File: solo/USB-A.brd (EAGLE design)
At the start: 43.8 x 16 mm, 26 parts, among them U1 USB_TRACES

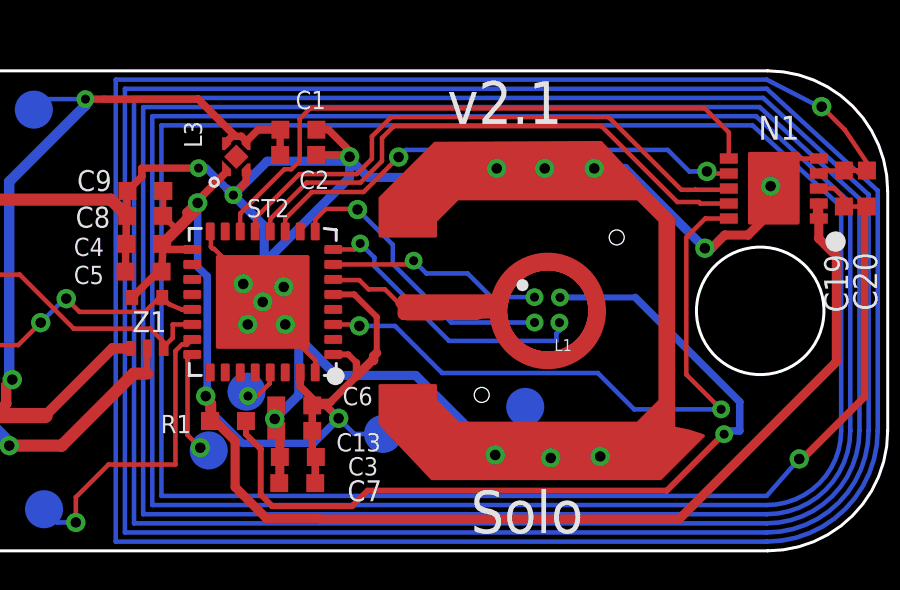
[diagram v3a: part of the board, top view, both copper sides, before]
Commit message: go back to using old LED
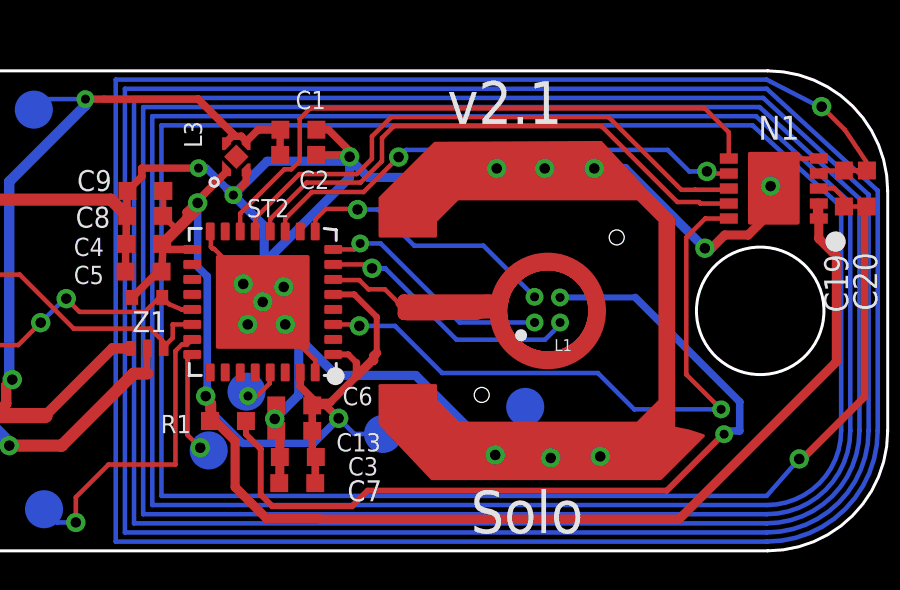
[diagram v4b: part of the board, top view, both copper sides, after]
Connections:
- net N$10: now also L1.P$2; no longer L1.P$3
- net N$13: now also L1.P$1; no longer L1.P$2
- net N$14: now also L1.P$3; no longer L1.P$1
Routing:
- net N$14: track 7.34 -> 9.46 mm
- net N$10: track 9.79 -> 7.89 mm
- net N$13: track 9.81 -> 9.08 mm
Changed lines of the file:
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@@
 </layers>
 <board>
-<fusionsync huburn="a.cGVyc29uYWw6dWUyYjdlZTY2" projecturn="a.cGVyc29uYWw6dWUyYjdlZTY2IzIwMTgwNDI5MTI5NzYxOTgx" f3durn="urn:adsk.wipprod:dm.lineage:j4HlS92DQ3aJOR3aA8LYVQ" pcbguid="4a57c918-3773-4eb5-941a-4639588bec0f" lastpulledtime="" lastsyncedchangeguid="8ec78108-e873-5518-f778-6aed3102f0ab"/>
+<fusionsync huburn="a.cGVyc29uYWw6dWUyYjdlZTY2" projecturn="a.cGVyc29uYWw6dWUyYjdlZTY2IzIwMTgwNDI5MTI5NzYxOTgx" f3durn="urn:adsk.wipprod:dm.lineage:j4HlS92DQ3aJOR3aA8LYVQ" pcbguid="4a57c918-3773-4eb5-941a-4639588bec0f" lastpulledtime="" lastsyncedchangeguid="35127d9d-d647-938f-e0ae-f05b0d64aa73"/>
 <plain>
 <rectangle x1="3.6" y1="49.05" x2="4.4" y2="49.25" layer="41"/>
@@
 <attribute name="NAME" x="20.415" y="51.685" size="0.7" layer="25" ratio="15" rot="R180"/>
 </element>
-<element name="L1" library="efm-fido" library_urn="urn:adsk.eagle:library:4245354" package="CL-505S-X-SD-T" package3d_urn="urn:adsk.eagle:package:4878740/7" value="RGB_LED_1X1CL-505S-X-SD-T" x="35.36" y="47.45" smashed="yes" rot="R180">
+<element name="L1" library="efm-fido" library_urn="urn:adsk.eagle:library:4245354" package="CL-505S-X-SD-T" package3d_urn="urn:adsk.eagle:package:4878740/8" value="RGB_LED_1X1CL-505S-X-SD-T" x="35.36" y="47.45" smashed="yes" rot="R180">
 <attribute name="NAME" x="35.76" y="46.05" size="0.4" layer="21" rot="R180"/>
 </element>
@@
 <wire x1="28.5" y1="49.04" x2="28.7" y2="49.24" width="0.1524" layer="1"/>
 <via x="28.7" y="49.24" extent="1-16" drill="0.3"/>
-<wire x1="28.7" y1="49.24" x2="28.78" y2="49.24" width="0.1524" layer="16"/>
-<via x="35.34" y="46.6" extent="1-16" drill="0.3"/>
-<wire x1="28.7" y1="49.24" x2="29.1714" y2="48.7686" width="0.1524" layer="16"/>
-<wire x1="29.1714" y1="48.7686" x2="29.1714" y2="48.48104375" width="0.1524" layer="16"/>
-<wire x1="29.1714" y1="48.48104375" x2="31.66244375" y2="45.99" width="0.1524" layer="16"/>
-<wire x1="31.66244375" y1="45.99" x2="35.24" y2="45.99" width="0.1524" layer="16"/>
-<wire x1="35.24" y1="45.99" x2="35.24" y2="46.24" width="0.1524" layer="16"/>
-<contactref element="L1" pad="P$3"/>
-<wire x1="35.24" y1="46.24" x2="35.34" y2="46.34" width="0.1524" layer="16"/>
-<wire x1="35.34" y1="46.34" x2="35.34" y2="46.6" width="0.1524" layer="16"/>
-<wire x1="35.36" y1="46.6" x2="35.34" y2="46.6" width="0.1524" layer="1"/>
+<via x="34.513" y="46.605" extent="1-16" drill="0.3"/>
+<contactref element="L1" pad="P$2"/>
+<wire x1="34.513" y1="46.605" x2="32.0157875" y2="46.605" width="0.1524" layer="16"/>
+<wire x1="32.0157875" y1="46.605" x2="29.3807875" y2="49.24" width="0.1524" layer="16"/>
+<wire x1="29.3807875" y1="49.24" x2="28.7" y2="49.24" width="0.1524" layer="16"/>
+<wire x1="34.513" y1="46.605" x2="34.51" y2="46.6" width="0" layer="19" extent="1-1"/>
 </signal>
 <signal name="N$13">
@@
 <via x="28.61" y="50.37" extent="1-16" drill="0.35"/>
 <wire x1="27.2" y1="49.64" x2="27.2" y2="50.04" width="0.1524" layer="1"/>
-<via x="34.512" y="46.604" extent="1-16" drill="0.3"/>
-<contactref element="L1" pad="P$2"/>
-<wire x1="28.61" y1="50.37" x2="29.7858" y2="49.1942" width="0.1524" layer="16"/>
-<wire x1="29.7858" y1="49.1942" x2="29.7858" y2="48.5545625" width="0.1524" layer="16"/>
-<wire x1="29.7858" y1="48.5545625" x2="31.7363625" y2="46.604" width="0.1524" layer="16"/>
-<wire x1="31.7363625" y1="46.604" x2="34.512" y2="46.604" width="0.1524" layer="16"/>
-<wire x1="34.512" y1="46.604" x2="34.51" y2="46.6" width="0" layer="19" extent="1-1"/>
+<via x="34.512" y="47.46" extent="1-16" drill="0.3"/>
+<wire x1="29.294" y1="50.37" x2="30.4998" y2="49.1642" width="0.1524" layer="16"/>
+<wire x1="28.61" y1="50.37" x2="29.294" y2="50.37" width="0.1524" layer="16"/>
+<contactref element="L1" pad="P$1"/>
+<wire x1="30.4998" y1="49.1642" x2="32.8078" y2="49.1642" width="0.1524" layer="16"/>
+<wire x1="32.8078" y1="49.1642" x2="34.512" y2="47.46" width="0.1524" layer="16"/>
+<wire x1="34.512" y1="47.46" x2="34.51" y2="47.45" width="0" layer="19" extent="1-1"/>
 </signal>
 <signal name="N$14">
 <contactref element="ST2" pad="7"/>
-<wire x1="27.8" y1="48.54" x2="30.481" y2="48.54" width="0.1524" layer="1"/>
-<wire x1="30.481" y1="48.54" x2="30.481" y2="48.664" width="0.1524" layer="1"/>
-<via x="30.481" y="48.664" extent="1-16" drill="0.3"/>
-<wire x1="30.481" y1="48.664" x2="30.905" y2="48.24" width="0.1524" layer="16"/>
-<wire x1="30.905" y1="48.24" x2="32.28" y2="48.24" width="0.1524" layer="16"/>
-<via x="34.509" y="47.45" extent="1-16" drill="0.3"/>
-<contactref element="L1" pad="P$1"/>
-<wire x1="32.28" y1="48.24" x2="33.07" y2="47.45" width="0.1524" layer="16"/>
-<wire x1="33.07" y1="47.45" x2="34.509" y2="47.45" width="0.1524" layer="16"/>
-<wire x1="34.509" y1="47.45" x2="34.51" y2="47.45" width="0" layer="19" extent="1-1"/>
+<via x="35.361" y="46.604" extent="1-16" drill="0.3"/>
+<contactref element="L1" pad="P$3"/>
+<wire x1="35.361" y1="46.604" x2="35.361" y2="46.5333625" width="0.1524" layer="16"/>
+<wire x1="35.361" y1="46.5333625" x2="34.8586375" y2="46.031" width="0.1524" layer="16"/>
+<wire x1="34.8586375" y1="46.031" x2="31.911" y2="46.031" width="0.1524" layer="16"/>
+<wire x1="29.547" y1="48.395" x2="29.414" y2="48.395" width="0.1524" layer="16"/>
+<wire x1="31.911" y1="46.031" x2="29.547" y2="48.395" width="0.1524" layer="16"/>
+<via x="29.093" y="48.412" extent="1-16" drill="0.35"/>
+<wire x1="27.8" y1="48.54" x2="28.8448" y2="48.54" width="0.1524" layer="1"/>
+<wire x1="28.8448" y1="48.54" x2="28.9149" y2="48.4699" width="0.1524" layer="1"/>
+<wire x1="28.9149" y1="48.4699" x2="29.0198" y2="48.365" width="0.1524" layer="1"/>
+<wire x1="29.093" y1="48.412" x2="29.0351" y2="48.4699" width="0.1524" layer="1"/>
+<wire x1="29.0351" y1="48.4699" x2="28.9149" y2="48.4699" width="0.1524" layer="1"/>
+<wire x1="29.093" y1="48.412" x2="28.965" y2="48.54" width="0.1524" layer="1"/>
+<wire x1="28.965" y1="48.54" x2="28.8448" y2="48.54" width="0.1524" layer="1"/>
+<wire x1="29.547" y1="48.395" x2="29.53" y2="48.412" width="0.1524" layer="16"/>
+<wire x1="29.53" y1="48.412" x2="29.093" y2="48.412" width="0.1524" layer="16"/>
+<wire x1="35.361" y1="46.604" x2="35.36" y2="46.6" width="0" layer="19" extent="1-1"/>
 </signal>
 <signal name="N$15">
